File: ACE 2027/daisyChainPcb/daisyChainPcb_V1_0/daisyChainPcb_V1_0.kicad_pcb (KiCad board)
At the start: 2 copper layers, 56.5 x 97 mm, 27 parts, among them J201 Pads, J202 XT30, J203 XT30, J204 Pads, J205 Pads, J206 RJ45, J207 RJ45, U101 AP7361C-33E-13

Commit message: Changed placement of TPs and size of vias for stitching
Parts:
- TP201, TP203: moved to B.Cu
- moved TP201 45.1 mm to (174.7, 55.3), turned to 180 degrees
- moved TP203 40.6 mm to (171.1, 55.3), turned to 180 degrees
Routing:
- net /Controle/CAN_N: track 70.8 -> 84.7 mm, vias 0 -> 1
- net /Controle/CAN_P: track 54.5 -> 65.3 mm, vias 1 -> 2
- net +48V: track 118.1 -> 115.3 mm, vias 4 -> 6
- net signal_GND: vias 2 -> 836

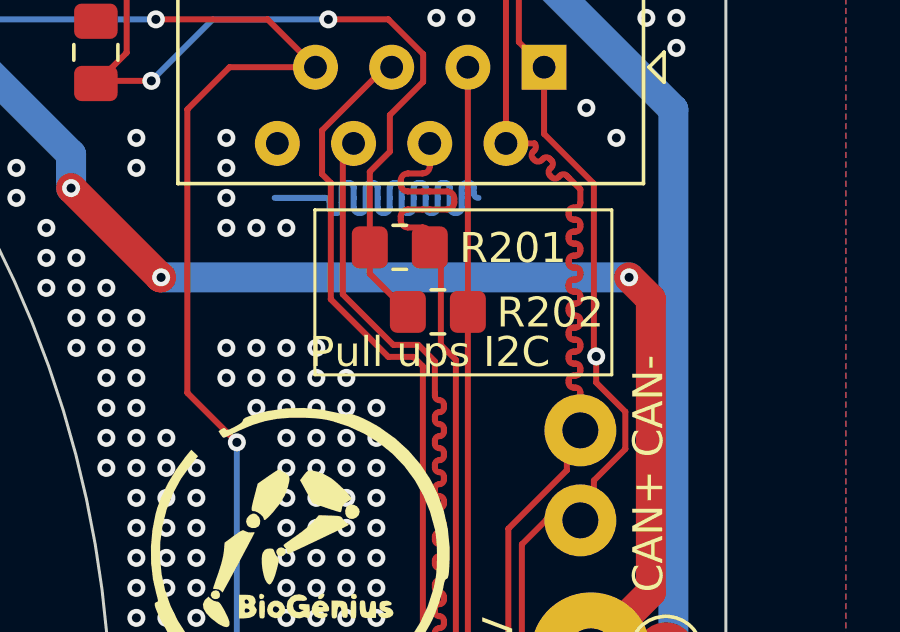
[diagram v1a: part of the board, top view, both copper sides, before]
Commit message: Corrected some DRC warnings and errors
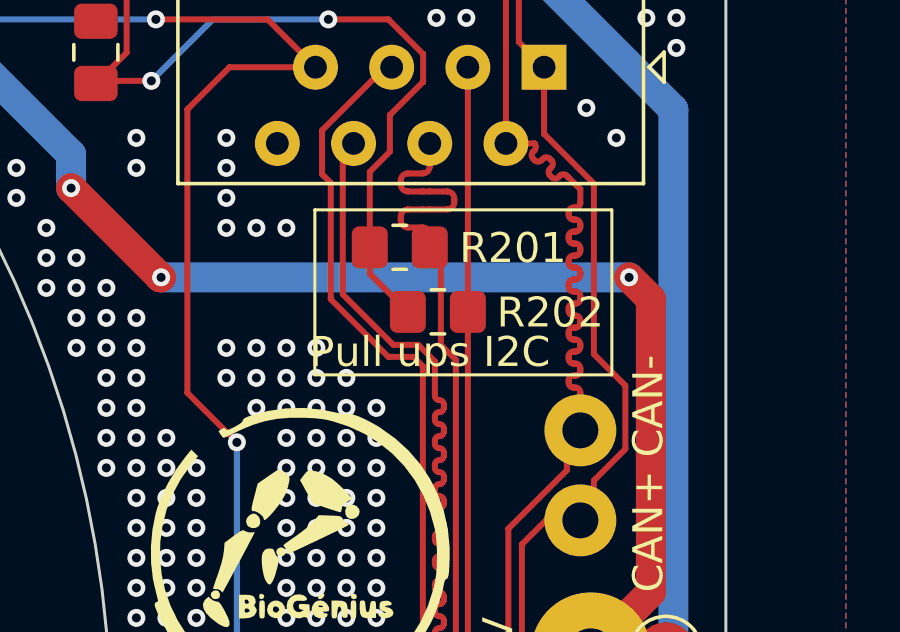
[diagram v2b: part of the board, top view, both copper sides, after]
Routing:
- net /Controle/CAN_N: track 84.7 -> 68.0 mm
- net /Controle/CAN_P: vias 2 -> 1

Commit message: version finale
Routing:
- net /Controle/CAN_P: track 65.3 -> 67.7 mm
